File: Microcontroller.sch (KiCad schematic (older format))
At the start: 24 parts

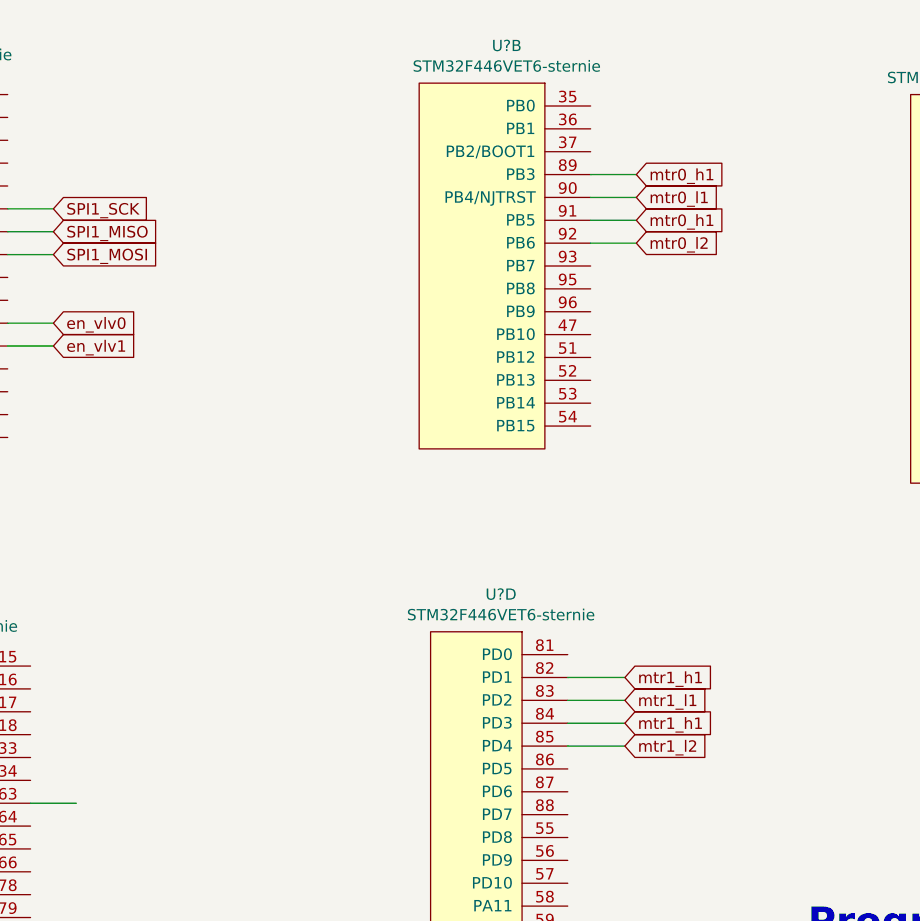
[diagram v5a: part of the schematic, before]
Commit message: Updated Motor Channels
Each motor only needs two inputs.
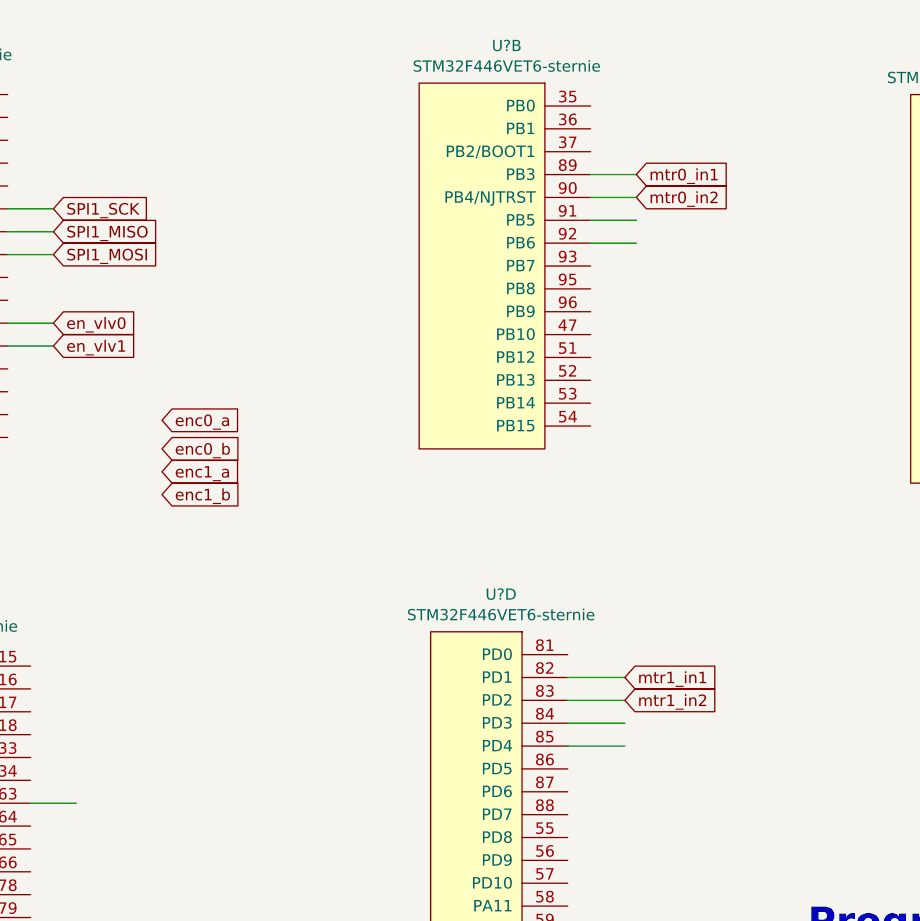
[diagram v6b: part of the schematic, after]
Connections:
- net labels added: enc0_a, enc0_b, enc1_a, enc1_b, mtr0_in1, mtr0_in2, mtr1_in1, mtr1_in2
- net labels removed: mtr0_h1, mtr0_l1, mtr0_l2, mtr1_h1, mtr1_l1, mtr1_l2
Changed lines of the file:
@@
 	2050 4400 1850 4400
 Text GLabel 4500 1650 2    50   Input ~ 0
-mtr0_h1
+mtr0_in1
 Text GLabel 4500 1750 2    50   Input ~ 0
-mtr0_l1
+mtr0_in2
 Wire Wire Line
 	4300 1650 4500 1650
@@
 	1    0    0    -1
 $EndComp
-Text GLabel 4500 1850 2    50   Input ~ 0
-mtr0_h1
-Text GLabel 4500 1950 2    50   Input ~ 0
-mtr0_l2
 Text GLabel 4450 3850 2    50   Input ~ 0
-mtr1_h1
+mtr1_in1
 Text GLabel 4450 3950 2    50   Input ~ 0
-mtr1_l1
-Text GLabel 4450 4050 2    50   Input ~ 0
-mtr1_h1
-Text GLabel 4450 4150 2    50   Input ~ 0
-mtr1_l2
+mtr1_in2
+Text GLabel 2425 2725 2    50   Input ~ 0
+enc0_a
+Text GLabel 2425 2850 2    50   Input ~ 0
+enc0_b
+Text GLabel 2425 2950 2    50   Input ~ 0
+enc1_a
+Text GLabel 2425 3050 2    50   Input ~ 0
+enc1_b
 $EndSCHEMATC

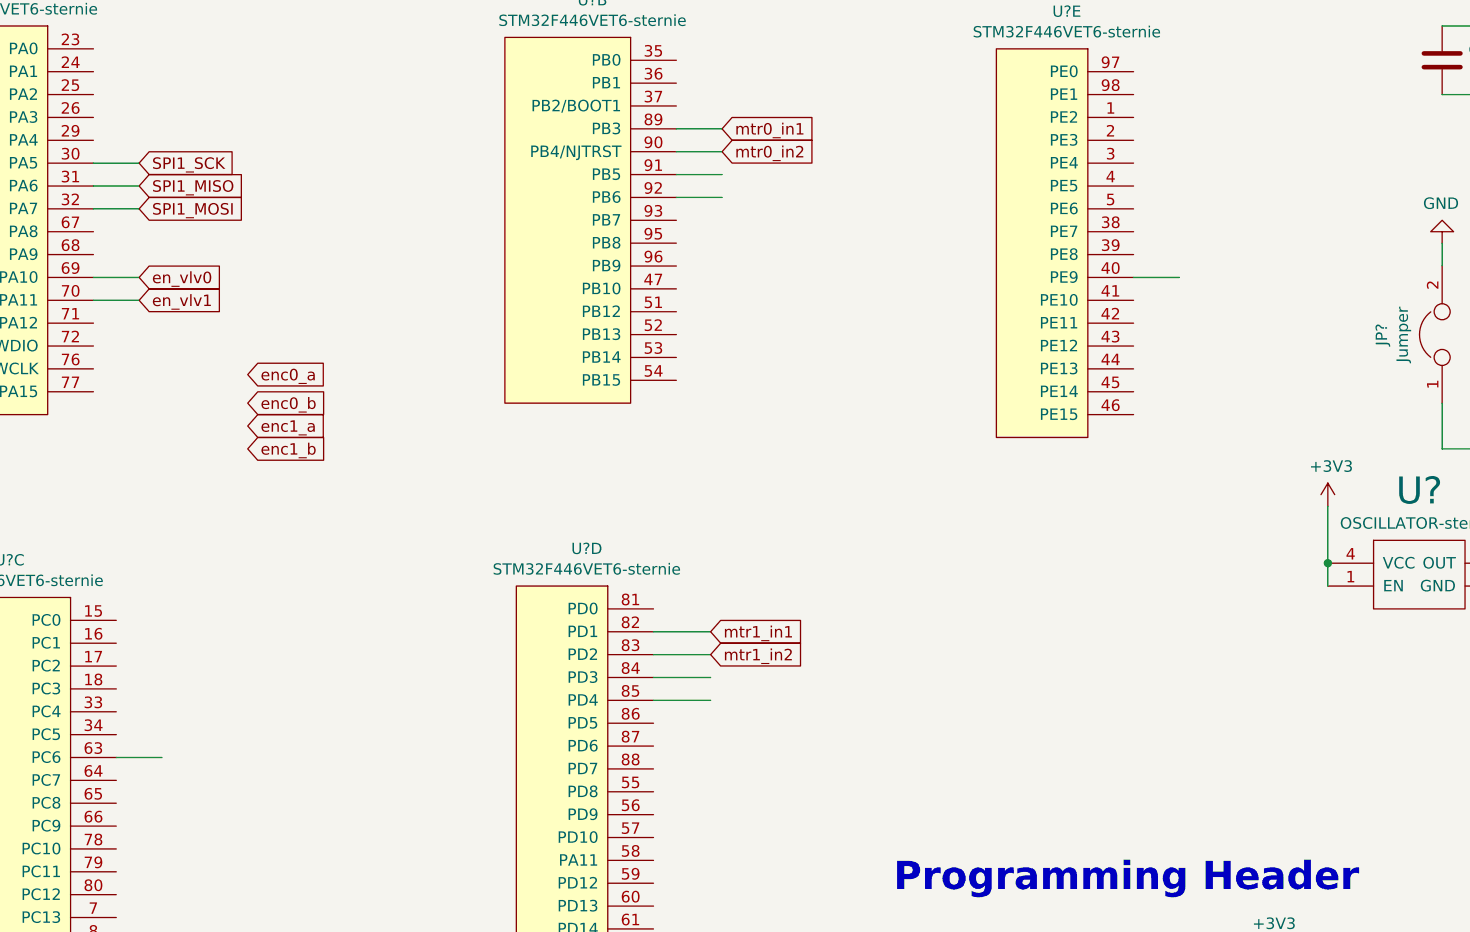
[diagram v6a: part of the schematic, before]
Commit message: added dual inpt and gate control
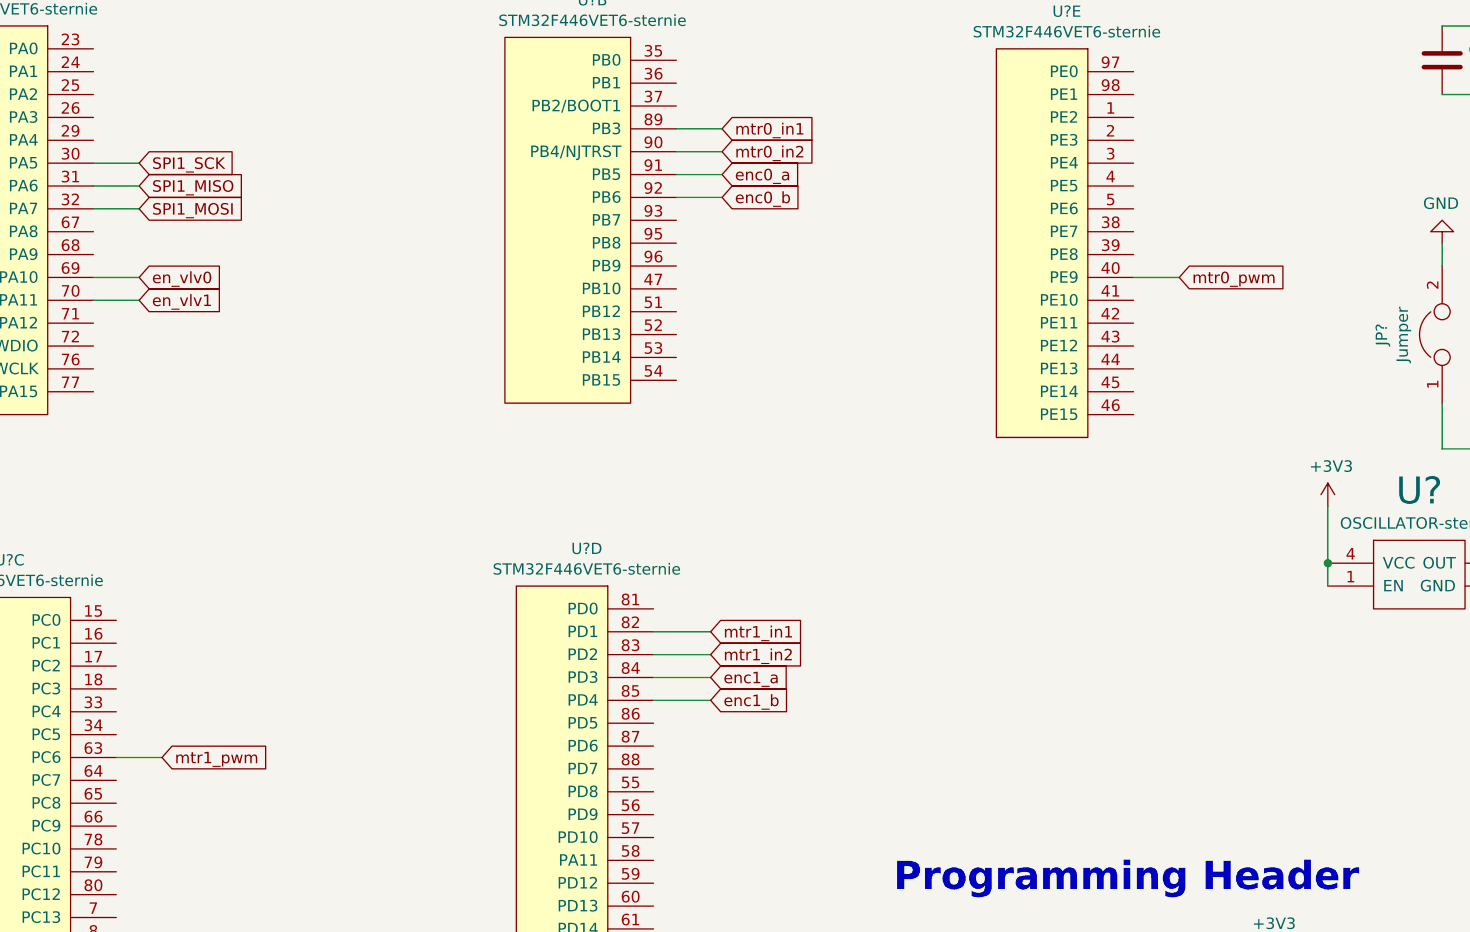
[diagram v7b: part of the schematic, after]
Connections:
- net labels added: mtr0_pwm, mtr1_pwm
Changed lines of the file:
@@
 	4300 1850 4500 1850
-Wire Wire Line
-	4300 1950 4500 1950
 Wire Wire Line
 	4200 3850 4450 3850
@@
 Text GLabel 4450 3950 2    50   Input ~ 0
 mtr1_in2
-Text GLabel 2425 2725 2    50   Input ~ 0
+Text GLabel 4500 1850 2    50   Input ~ 0
 enc0_a
-Text GLabel 2425 2850 2    50   Input ~ 0
+Text GLabel 4500 1950 2    50   Input ~ 0
 enc0_b
-Text GLabel 2425 2950 2    50   Input ~ 0
+Text GLabel 4450 4050 2    50   Input ~ 0
 enc1_a
-Text GLabel 2425 3050 2    50   Input ~ 0
+Text GLabel 4450 4150 2    50   Input ~ 0
 enc1_b
+Text GLabel 2050 4400 2    50   Input ~ 0
+mtr1_pwm
+Text GLabel 6500 2300 2    50   Input ~ 0
+mtr0_pwm
+Wire Wire Line
+	4300 1950 4500 1950
 $EndSCHEMATC

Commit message: Motor capacitors, test points, jumpers
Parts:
- added TP? (x3): TEST, symbol ec_2b_rescue:TEST
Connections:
- net SPI1_MISO: now also TP?.1
- net SPI1_MOSI: now also TP?.1
- net SPI1_SCK: now also TP?.1
- net led0: now reaches U?.65 (PC8)
- net led1: now reaches U?.66 (PC9)
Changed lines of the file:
@@
 $Descr A4 11693 8268
 encoding utf-8
-Sheet 8 12
+Sheet 7 12
 Title ""
 Date ""
@@
 Wire Wire Line
 	4300 1950 4500 1950
+Text GLabel 1850 4600 2    50   Input ~ 0
+led0
+Text GLabel 1850 4700 2    50   Input ~ 0
+led1
+Text GLabel 1450 6200 2    50   Input ~ 0
+SPI1_SCK
+Text GLabel 1450 6600 2    50   Input ~ 0
+SPI1_MISO
+Text GLabel 1450 6975 2    50   Input ~ 0
+SPI1_MOSI
+$Comp
+L ec_2b_rescue:TEST TP?
+U 1 1 5E750D41
+P 1450 6600
+F 0 "TP?" V 1528 6738 50  0000 L CNN
+F 1 "TEST" H 1528 6647 50  0001 L CNN
+F 2 "" H 1450 6600 50  0001 C CNN
+F 3 "" H 1450 6600 50  0001 C CNN
+	1    1450 6600
+	0    -1   -1   0
+$EndComp
+$Comp
+L ec_2b_rescue:TEST TP?
+U 1 1 5E750D4D
+P 1450 6975
+F 0 "TP?" V 1528 7113 50  0000 L CNN
+F 1 "TEST" H 1528 7022 50  0001 L CNN
+F 2 "" H 1450 6975 50  0001 C CNN
+F 3 "" H 1450 6975 50  0001 C CNN
+	1    1450 6975
+	0    -1   -1   0
+$EndComp
+$Comp
+L ec_2b_rescue:TEST TP?
+U 1 1 5E750D47
+P 1450 6200
+F 0 "TP?" V 1528 6338 50  0000 L CNN
+F 1 "TEST" H 1528 6247 50  0001 L CNN
+F 2 "" H 1450 6200 50  0001 C CNN
+F 3 "" H 1450 6200 50  0001 C CNN
+	1    1450 6200
+	0    -1   -1   0
+$EndComp
 $EndSCHEMATC
